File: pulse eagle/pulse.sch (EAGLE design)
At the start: 24 parts, among them IC1 LM358D, J1 ISP Touch, T1 BC846, Y1 8MHz

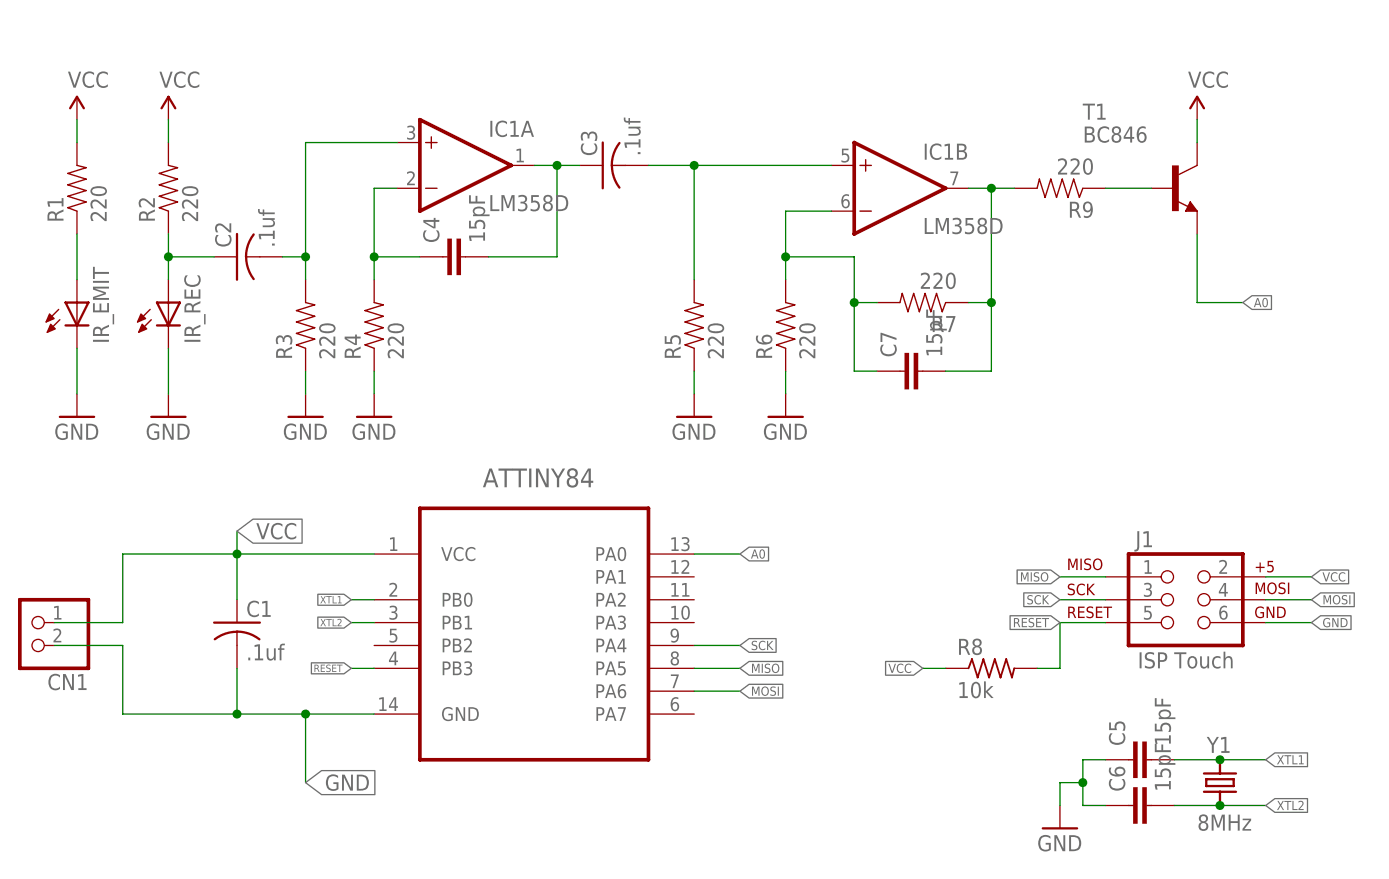
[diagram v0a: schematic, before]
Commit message: Finished board layout at .8"x1.25". Needs labels, then it's ready to print!
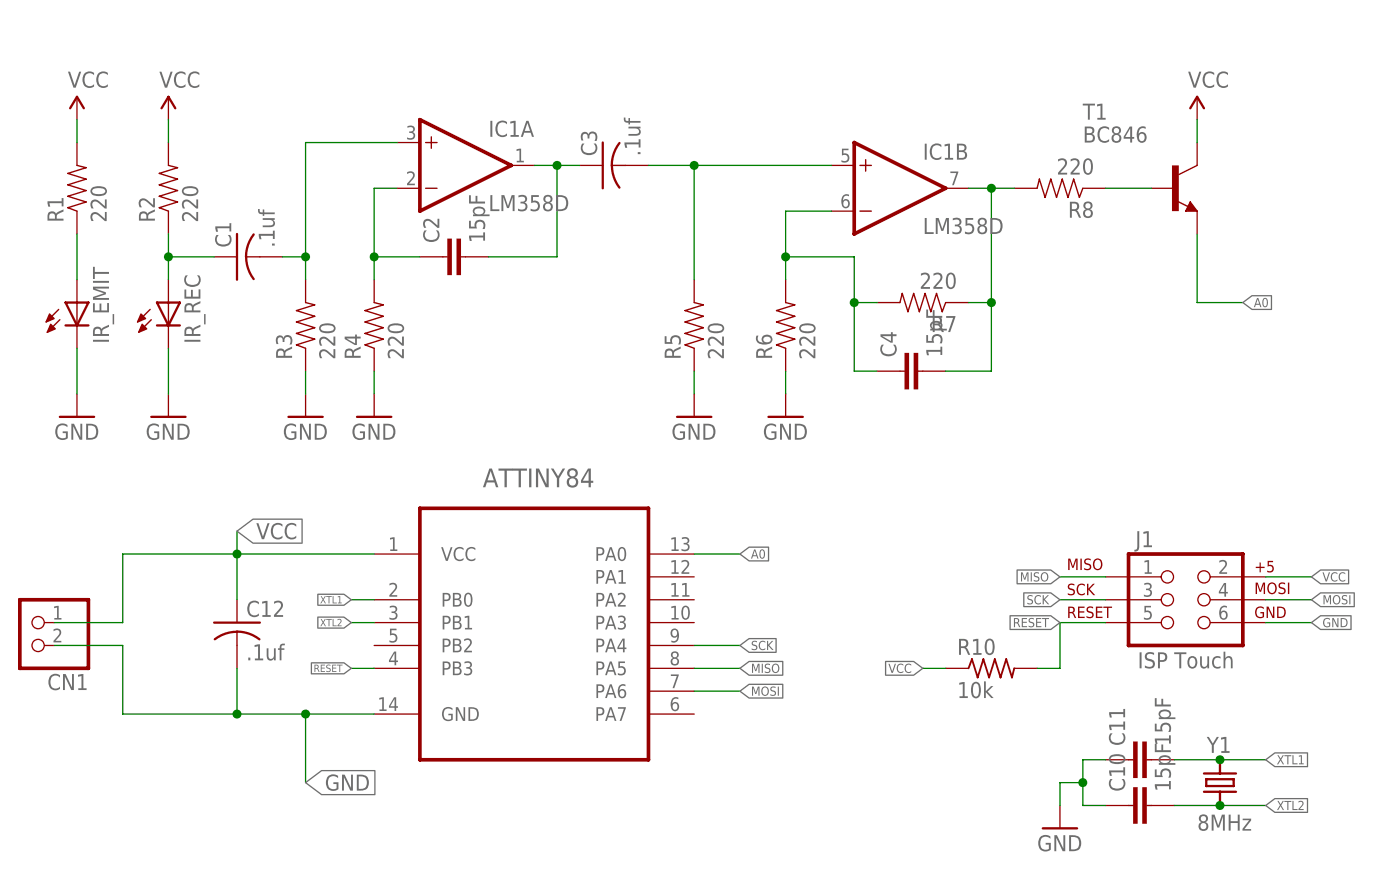
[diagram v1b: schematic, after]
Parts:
- removed C7: 15pF, SparkFun-Passives:CAP0805
- removed R9: 220, SparkFun-Resistors:220-5%
- added C12: .1uf, adafruit:C-USC0805
- added R10: 10k, adafruit:R-US_R0805
- C2: value .1uf -> 15pF; device adafruit:C-USC0805 -> SparkFun-Passives:CAP0805
- R8: value 10k -> 220; device adafruit:R-US_R0805 -> SparkFun-Resistors:220-5%
- renumbered C5 to C11, C6 to C10
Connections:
- net GND: now also C12.2; no longer C1.2
- net N$2: now also C1.1; no longer C2.1
- net N$3: now also C1.2; no longer C2.2
- net N$4: now also C2.1; no longer C4.1
- net N$5: now also C2.2; no longer C4.2
- net N$7: now also C4.1; no longer C7.1
- net N$8: now also C4.2, R8.2; no longer C7.2, R9.2
- net N$9: now also R8.1; no longer R9.1
- net RESET: now also R10.2; no longer R8.2
- net VCC: now also C12.1, R10.1; no longer C1.1, R8.1
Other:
- moved on the sheet: C1, C2, C4, R8
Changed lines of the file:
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@@
 <parts>
 <part name="ATTINY84" library="Atmel_By_element14_Batch_1" deviceset="ATTINY84-20SSU" device="" value=""/>
-<part name="C1" library="adafruit" deviceset="C-US" device="C0805" value=".1uf"/>
-<part name="R8" library="adafruit" deviceset="R-US_" device="R0805" value="10k"/>
+<part name="C12" library="adafruit" deviceset="C-US" device="C0805" value=".1uf"/>
+<part name="R10" library="adafruit" deviceset="R-US_" device="R0805" value="10k"/>
 <part name="Y1" library="remote" deviceset="CRYSTAL" device="" value="8MHz"/>
 <part name="GND3" library="SparkFun" deviceset="GND" device=""/>
-<part name="C5" library="SparkFun-Passives" deviceset="CAP" device="0805" value="15pF"/>
-<part name="C6" library="SparkFun-Passives" deviceset="CAP" device="0805" value="15pF"/>
+<part name="C11" library="SparkFun-Passives" deviceset="CAP" device="0805" value="15pF"/>
+<part name="C10" library="SparkFun-Passives" deviceset="CAP" device="0805" value="15pF"/>
 <part name="J1" library="remote" deviceset="ISPTOUCH" device="_HEADER" value="ISP Touch"/>
 <part name="CN1" library="adafruit" deviceset="JST_2PIN" device="-THM"/>
@@
 <part name="R6" library="SparkFun-Resistors" deviceset="220-5%" device="" value="220"/>
 <part name="R7" library="SparkFun-Resistors" deviceset="220-5%" device="" value="220"/>
-<part name="R9" library="SparkFun-Resistors" deviceset="220-5%" device="" value="220"/>
-<part name="C2" library="adafruit" deviceset="C-US" device="C0805" value=".1uf"/>
+<part name="R8" library="SparkFun-Resistors" deviceset="220-5%" device="" value="220"/>
+<part name="C1" library="adafruit" deviceset="C-US" device="C0805" value=".1uf"/>
 <part name="C3" library="adafruit" deviceset="C-US" device="C0805" value=".1uf"/>
+<part name="C2" library="SparkFun-Passives" deviceset="CAP" device="0805" value="15pF"/>
 <part name="C4" library="SparkFun-Passives" deviceset="CAP" device="0805" value="15pF"/>
-<part name="C7" library="SparkFun-Passives" deviceset="CAP" device="0805" value="15pF"/>
 <part name="T1" library="transistor" deviceset="BC846" device=""/>
 <part name="IC1" library="linear" deviceset="LM358" device="D"/>
@@
 <instances>
 <instance part="ATTINY84" gate="A" x="60.96" y="27.94"/>
-<instance part="C1" gate="G$1" x="27.94" y="25.4"/>
-<instance part="R8" gate="G$1" x="111.76" y="20.32"/>
+<instance part="C12" gate="G$1" x="27.94" y="25.4"/>
+<instance part="R10" gate="G$1" x="111.76" y="20.32"/>
 <instance part="Y1" gate="G$1" x="137.16" y="7.62" smashed="yes" rot="R90">
 <attribute name="NAME" x="138.43" y="12.7" size="1.778" layer="95" rot="R180"/>
@@
 </instance>
 <instance part="GND3" gate="1" x="119.38" y="2.54"/>
-<instance part="C5" gate="G$1" x="129.54" y="10.16" rot="R90"/>
-<instance part="C6" gate="G$1" x="129.54" y="5.08" rot="R90"/>
+<instance part="C11" gate="G$1" x="129.54" y="10.16" rot="R90"/>
+<instance part="C10" gate="G$1" x="129.54" y="5.08" rot="R90"/>
 <instance part="J1" gate="G$1" x="132.08" y="27.94"/>
 <instance part="CN1" gate="G$1" x="5.08" y="25.4" rot="R180"/>
@@
 <instance part="R6" gate="G$1" x="88.9" y="58.42" rot="R90"/>
 <instance part="R7" gate="G$1" x="104.14" y="60.96" rot="R180"/>
-<instance part="R9" gate="G$1" x="119.38" y="73.66" rot="R180"/>
-<instance part="C2" gate="G$1" x="27.94" y="66.04" rot="R90"/>
+<instance part="R8" gate="G$1" x="119.38" y="73.66" rot="R180"/>
+<instance part="C1" gate="G$1" x="27.94" y="66.04" rot="R90"/>
 <instance part="C3" gate="G$1" x="68.58" y="76.2" rot="R90"/>
-<instance part="C4" gate="G$1" x="53.34" y="66.04" rot="R90"/>
-<instance part="C7" gate="G$1" x="104.14" y="53.34" rot="R90"/>
+<instance part="C2" gate="G$1" x="53.34" y="66.04" rot="R90"/>
+<instance part="C4" gate="G$1" x="104.14" y="53.34" rot="R90"/>
 <instance part="T1" gate="G$1" x="132.08" y="73.66"/>
 <instance part="IC1" gate="A" x="53.34" y="76.2"/>
@@
 <wire x1="35.56" y1="15.24" x2="35.56" y2="7.62" width="0.1524" layer="91"/>
 <label x="35.56" y="7.62" size="1.778" layer="95" xref="yes"/>
-<pinref part="C1" gate="G$1" pin="2"/>
+<pinref part="C12" gate="G$1" pin="2"/>
 <wire x1="27.94" y1="20.32" x2="27.94" y2="15.24" width="0.1524" layer="91"/>
 <junction x="35.56" y="15.24"/>
@@
 <junction x="121.92" y="7.62"/>
 <pinref part="GND3" gate="1" pin="GND"/>
-<pinref part="C5" gate="G$1" pin="1"/>
-<pinref part="C6" gate="G$1" pin="1"/>
+<pinref part="C11" gate="G$1" pin="1"/>
+<pinref part="C10" gate="G$1" pin="1"/>
 </segment>
 <segment>
@@
 <segment>
 <pinref part="ATTINY84" gate="A" pin="VCC"/>
-<pinref part="C1" gate="G$1" pin="1"/>
+<pinref part="C12" gate="G$1" pin="1"/>
 <wire x1="43.18" y1="33.02" x2="27.94" y2="33.02" width="0.1524" layer="91"/>
 <wire x1="27.94" y1="33.02" x2="27.94" y2="27.94" width="0.1524" layer="91"/>
@@
 </segment>
 <segment>
-<pinref part="R8" gate="G$1" pin="1"/>
+<pinref part="R10" gate="G$1" pin="1"/>
 <wire x1="106.68" y1="20.32" x2="104.14" y2="20.32" width="0.1524" layer="91"/>
 <label x="104.14" y="20.32" size="1.016" layer="95" rot="R180" xref="yes"/>
@@
 <label x="119.38" y="25.4" size="1.016" layer="95" rot="R180" xref="yes"/>
 <wire x1="119.38" y1="25.4" x2="119.38" y2="20.32" width="0.1524" layer="91"/>
-<pinref part="R8" gate="G$1" pin="2"/>
+<pinref part="R10" gate="G$1" pin="2"/>
 <wire x1="119.38" y1="20.32" x2="116.84" y2="20.32" width="0.1524" layer="91"/>
 </segment>
@@
 <pinref part="Y1" gate="G$1" pin="2"/>
 <label x="142.24" y="10.16" size="1.016" layer="95" xref="yes"/>
-<pinref part="C5" gate="G$1" pin="2"/>
+<pinref part="C11" gate="G$1" pin="2"/>
 </segment>
 <segment>
@@
 <pinref part="Y1" gate="G$1" pin="1"/>
 <label x="142.24" y="5.08" size="1.016" layer="95" xref="yes"/>
-<pinref part="C6" gate="G$1" pin="2"/>
+<pinref part="C10" gate="G$1" pin="2"/>
 </segment>
 <segment>
@@
 <pinref part="IR_REC" gate="G$1" pin="A"/>
 <wire x1="20.32" y1="68.58" x2="20.32" y2="66.04" width="0.1524" layer="91"/>
-<pinref part="C2" gate="G$1" pin="1"/>
+<pinref part="C1" gate="G$1" pin="1"/>
 <wire x1="20.32" y1="66.04" x2="20.32" y2="63.5" width="0.1524" layer="91"/>
 <wire x1="20.32" y1="66.04" x2="25.4" y2="66.04" width="0.1524" layer="91"/>
@@
 <net name="N$3" class="0">
 <segment>
-<pinref part="C2" gate="G$1" pin="2"/>
+<pinref part="C1" gate="G$1" pin="2"/>
 <pinref part="R3" gate="G$1" pin="2"/>
 <wire x1="33.02" y1="66.04" x2="35.56" y2="66.04" width="0.1524" layer="91"/>
@@
 <pinref part="R4" gate="G$1" pin="2"/>
 <wire x1="43.18" y1="73.66" x2="43.18" y2="66.04" width="0.1524" layer="91"/>
-<pinref part="C4" gate="G$1" pin="1"/>
+<pinref part="C2" gate="G$1" pin="1"/>
 <wire x1="43.18" y1="66.04" x2="43.18" y2="63.5" width="0.1524" layer="91"/>
 <wire x1="43.18" y1="66.04" x2="48.26" y2="66.04" width="0.1524" layer="91"/>
@@
 <net name="N$5" class="0">
 <segment>
-<pinref part="C4" gate="G$1" pin="2"/>
+<pinref part="C2" gate="G$1" pin="2"/>
 <wire x1="55.88" y1="66.04" x2="63.5" y2="66.04" width="0.1524" layer="91"/>
 <wire x1="63.5" y1="66.04" x2="63.5" y2="76.2" width="0.1524" layer="91"/>
@@
 <wire x1="96.52" y1="60.96" x2="96.52" y2="53.34" width="0.1524" layer="91"/>
 <junction x="96.52" y="60.96"/>
-<pinref part="C7" gate="G$1" pin="1"/>
+<pinref part="C4" gate="G$1" pin="1"/>
 <wire x1="96.52" y1="53.34" x2="99.06" y2="53.34" width="0.1524" layer="91"/>
 </segment>
@@
 <net name="N$8" class="0">
 <segment>
-<pinref part="C7" gate="G$1" pin="2"/>
+<pinref part="C4" gate="G$1" pin="2"/>
 <wire x1="106.68" y1="53.34" x2="111.76" y2="53.34" width="0.1524" layer="91"/>
 <wire x1="111.76" y1="53.34" x2="111.76" y2="60.96" width="0.1524" layer="91"/>
@@
 <wire x1="111.76" y1="60.96" x2="111.76" y2="73.66" width="0.1524" layer="91"/>
 <wire x1="111.76" y1="73.66" x2="109.22" y2="73.66" width="0.1524" layer="91"/>
-<pinref part="R9" gate="G$1" pin="2"/>
+<pinref part="R8" gate="G$1" pin="2"/>
 <wire x1="111.76" y1="73.66" x2="114.3" y2="73.66" width="0.1524" layer="91"/>
 <junction x="111.76" y="73.66"/>
@@
 <net name="N$9" class="0">
 <segment>
-<pinref part="R9" gate="G$1" pin="1"/>
+<pinref part="R8" gate="G$1" pin="1"/>
 <pinref part="T1" gate="G$1" pin="B"/>
 <wire x1="124.46" y1="73.66" x2="129.54" y2="73.66" width="0.1524" layer="91"/>

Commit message: Invoking power/ground on op amp, fixing dimension, drawing polarized lines for tantalum caps, and adjusting labels.
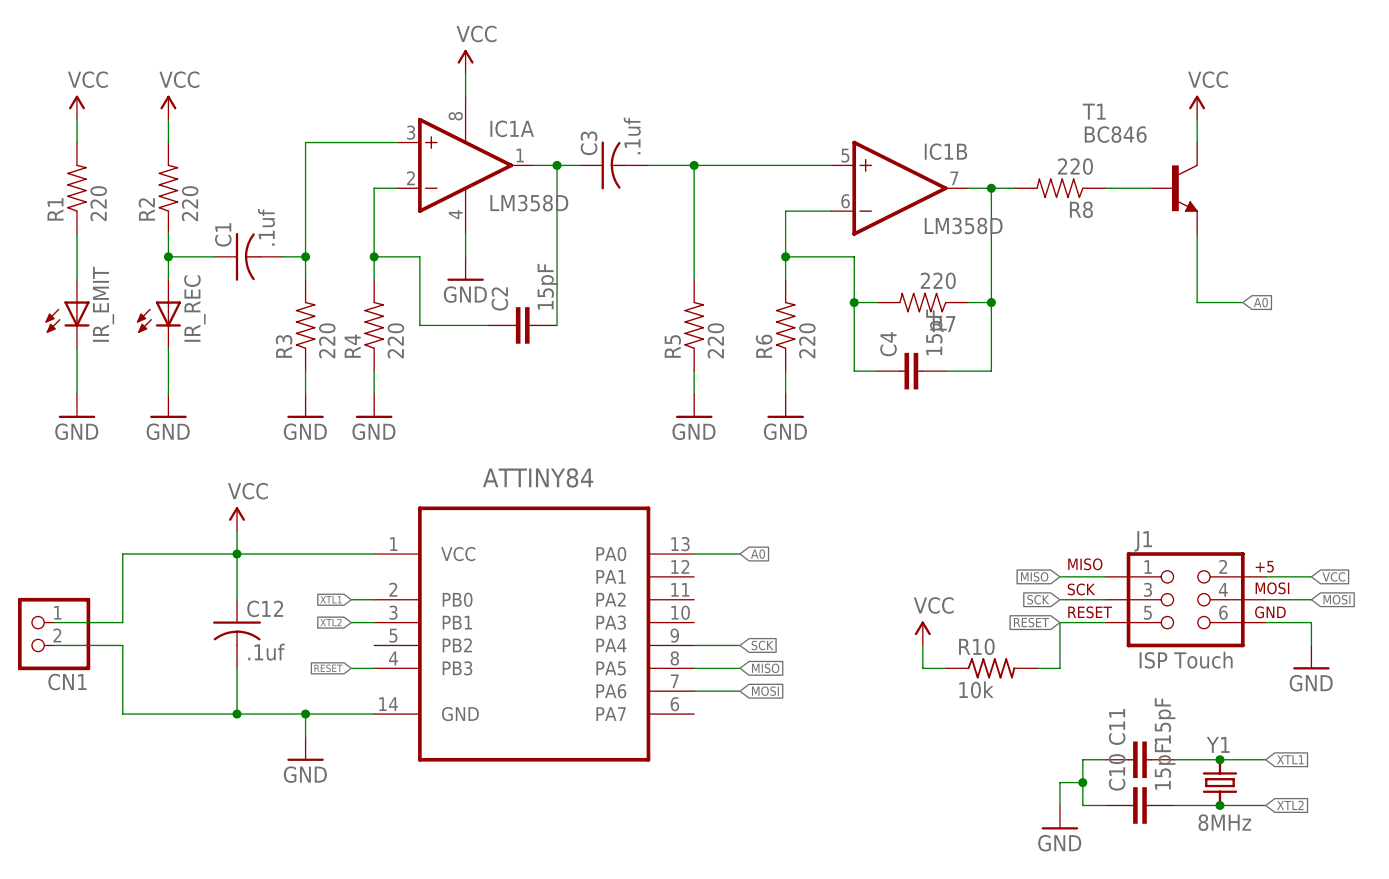
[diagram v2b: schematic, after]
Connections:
- net GND: now also IC1P.V-
- net VCC: now also IC1P.V+
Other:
- moved on the sheet: C2
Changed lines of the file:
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@@
 <part name="SUPPLY2" library="SparkFun-Aesthetics" deviceset="VCC" device=""/>
 <part name="SUPPLY3" library="SparkFun-Aesthetics" deviceset="VCC" device=""/>
+<part name="GND8" library="SparkFun" deviceset="GND" device=""/>
+<part name="SUPPLY4" library="SparkFun-Aesthetics" deviceset="VCC" device=""/>
+<part name="SUPPLY5" library="SparkFun-Aesthetics" deviceset="VCC" device=""/>
+<part name="GND9" library="SparkFun" deviceset="GND" device=""/>
+<part name="SUPPLY6" library="SparkFun-Aesthetics" deviceset="VCC" device=""/>
+<part name="GND10" library="SparkFun" deviceset="GND" device=""/>
 </parts>
 <sheets>
@@
 <instance part="C1" gate="G$1" x="27.94" y="66.04" rot="R90"/>
 <instance part="C3" gate="G$1" x="68.58" y="76.2" rot="R90"/>
-<instance part="C2" gate="G$1" x="53.34" y="66.04" rot="R90"/>
+<instance part="C2" gate="G$1" x="60.96" y="58.42" rot="R90"/>
 <instance part="C4" gate="G$1" x="104.14" y="53.34" rot="R90"/>
 <instance part="T1" gate="G$1" x="132.08" y="73.66"/>
@@
 <instance part="SUPPLY2" gate="1" x="20.32" y="81.28"/>
 <instance part="SUPPLY3" gate="1" x="134.62" y="81.28"/>
+<instance part="IC1" gate="P" x="53.34" y="76.2"/>
+<instance part="GND8" gate="1" x="53.34" y="63.5"/>
+<instance part="SUPPLY4" gate="1" x="53.34" y="86.36"/>
+<instance part="SUPPLY5" gate="1" x="27.94" y="35.56"/>
+<instance part="GND9" gate="1" x="35.56" y="10.16"/>
+<instance part="SUPPLY6" gate="1" x="104.14" y="22.86"/>
+<instance part="GND10" gate="1" x="147.32" y="20.32"/>
 </instances>
 <busses>
@@
 <pinref part="ATTINY84" gate="A" pin="GND"/>
 <wire x1="43.18" y1="15.24" x2="35.56" y2="15.24" width="0.1524" layer="91"/>
-<wire x1="35.56" y1="15.24" x2="35.56" y2="7.62" width="0.1524" layer="91"/>
-<label x="35.56" y="7.62" size="1.778" layer="95" xref="yes"/>
+<wire x1="35.56" y1="15.24" x2="35.56" y2="12.7" width="0.1524" layer="91"/>
 <pinref part="C12" gate="G$1" pin="2"/>
 <wire x1="27.94" y1="20.32" x2="27.94" y2="15.24" width="0.1524" layer="91"/>
@@
 <pinref part="CN1" gate="G$1" pin="1"/>
 <wire x1="15.24" y1="22.86" x2="7.62" y2="22.86" width="0.1524" layer="91"/>
+<pinref part="GND9" gate="1" pin="GND"/>
 </segment>
 <segment>
@@
 </segment>
 <segment>
-<pinref part="J1" gate="G$1" pin="6"/>
-<wire x1="142.24" y1="25.4" x2="147.32" y2="25.4" width="0.1524" layer="91"/>
-<label x="147.32" y="25.4" size="1.016" layer="95" xref="yes"/>
-</segment>
-<segment>
 <pinref part="R3" gate="G$1" pin="1"/>
 <pinref part="GND4" gate="1" pin="GND"/>
@@
 <pinref part="GND7" gate="1" pin="GND"/>
 <wire x1="88.9" y1="53.34" x2="88.9" y2="50.8" width="0.1524" layer="91"/>
+</segment>
+<segment>
+<pinref part="IC1" gate="P" pin="V-"/>
+<pinref part="GND8" gate="1" pin="GND"/>
+<wire x1="53.34" y1="68.58" x2="53.34" y2="66.04" width="0.1524" layer="91"/>
+</segment>
+<segment>
+<pinref part="J1" gate="G$1" pin="6"/>
+<pinref part="GND10" gate="1" pin="GND"/>
+<wire x1="142.24" y1="25.4" x2="147.32" y2="25.4" width="0.1524" layer="91"/>
+<wire x1="147.32" y1="25.4" x2="147.32" y2="22.86" width="0.1524" layer="91"/>
 </segment>
 </net>
@@
 <wire x1="27.94" y1="33.02" x2="27.94" y2="35.56" width="0.1524" layer="91"/>
 <junction x="27.94" y="33.02"/>
-<label x="27.94" y="35.56" size="1.778" layer="95" xref="yes"/>
 <wire x1="27.94" y1="33.02" x2="15.24" y2="33.02" width="0.1524" layer="91"/>
 <wire x1="15.24" y1="33.02" x2="15.24" y2="25.4" width="0.1524" layer="91"/>
 <pinref part="CN1" gate="G$1" pin="2"/>
 <wire x1="15.24" y1="25.4" x2="7.62" y2="25.4" width="0.1524" layer="91"/>
+<pinref part="SUPPLY5" gate="1" pin="VCC"/>
 </segment>
 <segment>
@@
 <pinref part="R10" gate="G$1" pin="1"/>
 <wire x1="106.68" y1="20.32" x2="104.14" y2="20.32" width="0.1524" layer="91"/>
-<label x="104.14" y="20.32" size="1.016" layer="95" rot="R180" xref="yes"/>
+<pinref part="SUPPLY6" gate="1" pin="VCC"/>
+<wire x1="104.14" y1="20.32" x2="104.14" y2="22.86" width="0.1524" layer="91"/>
 </segment>
 <segment>
@@
 <pinref part="T1" gate="G$1" pin="C"/>
 <wire x1="134.62" y1="81.28" x2="134.62" y2="78.74" width="0.1524" layer="91"/>
+</segment>
+<segment>
+<pinref part="IC1" gate="P" pin="V+"/>
+<pinref part="SUPPLY4" gate="1" pin="VCC"/>
+<wire x1="53.34" y1="83.82" x2="53.34" y2="86.36" width="0.1524" layer="91"/>
 </segment>
 </net>
@@
 <wire x1="43.18" y1="66.04" x2="43.18" y2="63.5" width="0.1524" layer="91"/>
 <wire x1="43.18" y1="66.04" x2="48.26" y2="66.04" width="0.1524" layer="91"/>
+<wire x1="48.26" y1="66.04" x2="48.26" y2="58.42" width="0.1524" layer="91"/>
+<wire x1="48.26" y1="58.42" x2="55.88" y2="58.42" width="0.1524" layer="91"/>
 <junction x="43.18" y="66.04"/>
 </segment>
@@
 <segment>
 <pinref part="C2" gate="G$1" pin="2"/>
-<wire x1="55.88" y1="66.04" x2="63.5" y2="66.04" width="0.1524" layer="91"/>
-<wire x1="63.5" y1="66.04" x2="63.5" y2="76.2" width="0.1524" layer="91"/>
+<wire x1="63.5" y1="58.42" x2="63.5" y2="76.2" width="0.1524" layer="91"/>
 <pinref part="IC1" gate="A" pin="OUT"/>
 <wire x1="63.5" y1="76.2" x2="60.96" y2="76.2" width="0.1524" layer="91"/>
